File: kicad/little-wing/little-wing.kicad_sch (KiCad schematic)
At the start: 0 parts

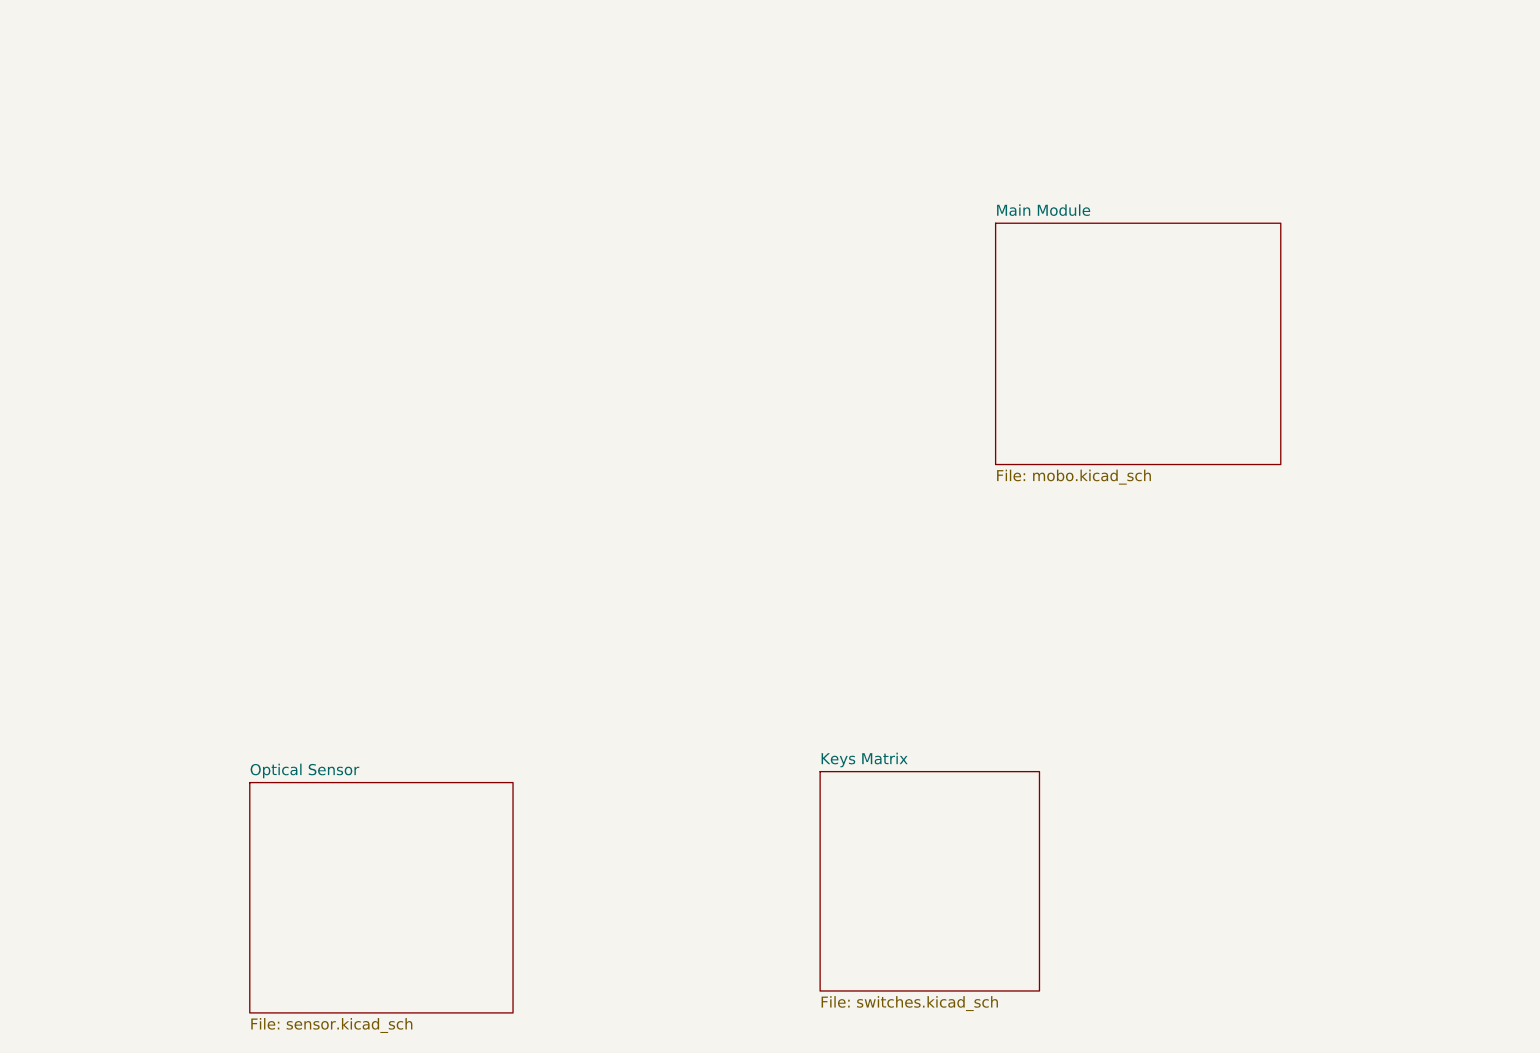
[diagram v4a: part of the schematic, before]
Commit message: Re-organising the schematics sheets a bit
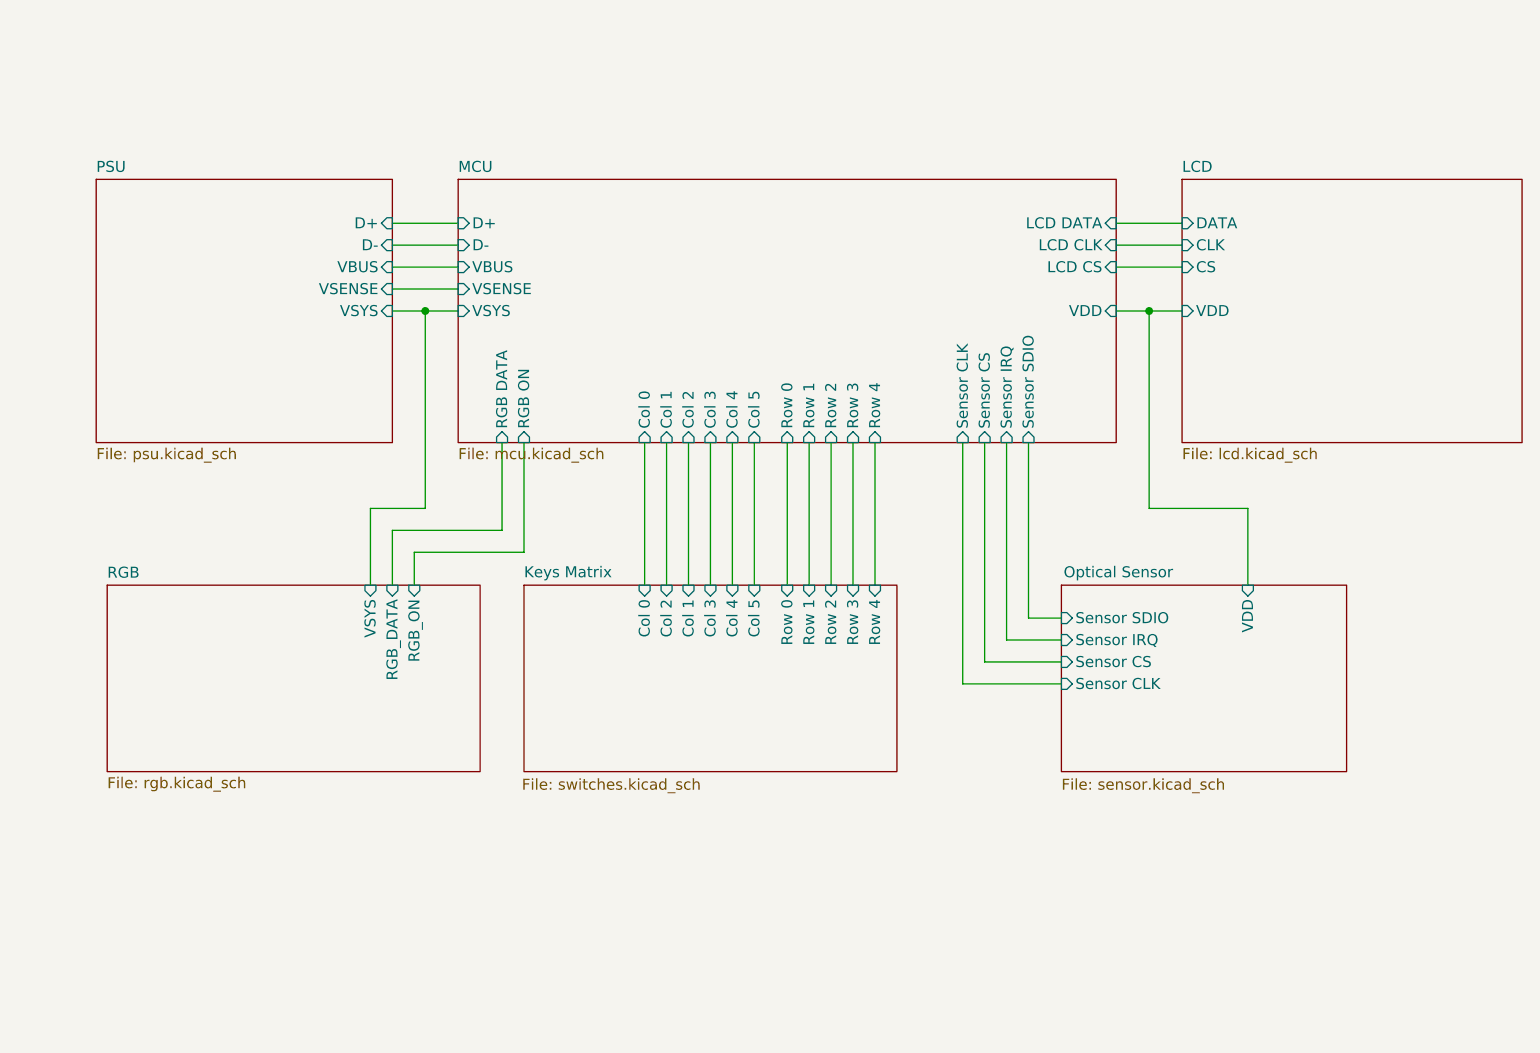
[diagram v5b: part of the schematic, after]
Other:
- removed sheet Main Module
- added sheet LCD (lcd.kicad_sch)
- added sheet MCU (mcu.kicad_sch)
- added sheet PSU (psu.kicad_sch)
- added sheet RGB (rgb.kicad_sch)
- sheet Keys Matrix ports: added Col 0, Col 1, Col 2, Col 3, Col 4, Col 5, Row 0, Row 1, Row 2, Row 3, Row 4; removed none
- sheet Optical Sensor ports: added Sensor CLK, Sensor CS, Sensor IRQ, Sensor SDIO, VDD; removed none

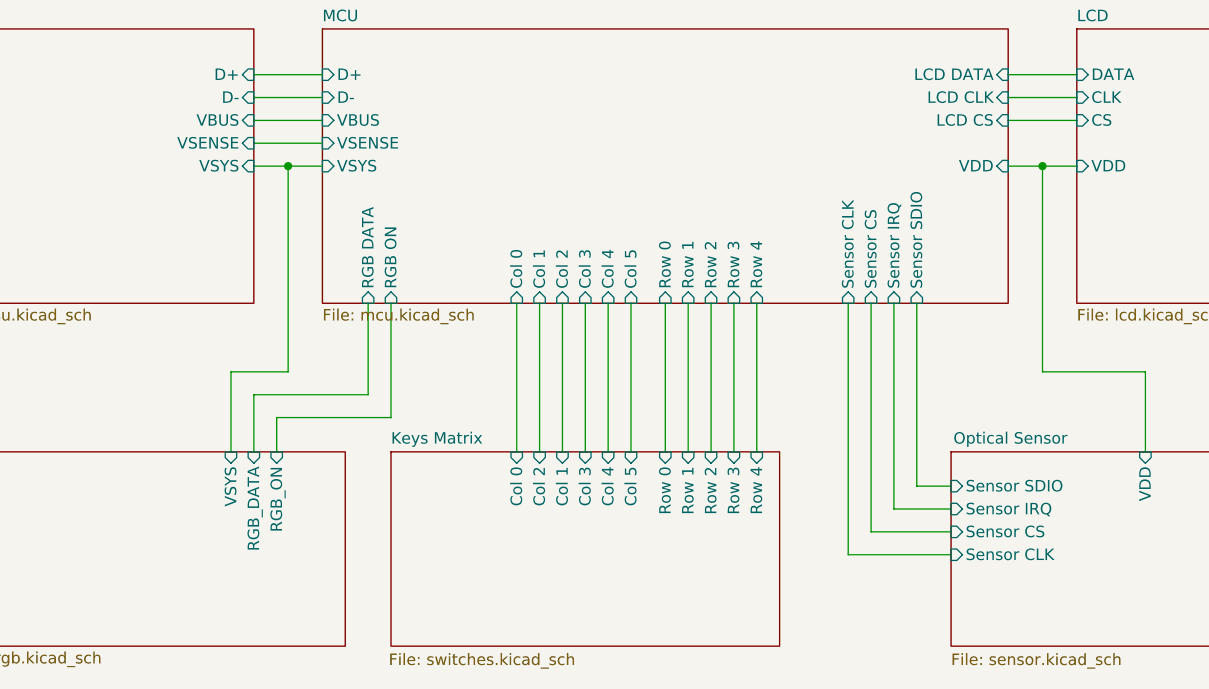
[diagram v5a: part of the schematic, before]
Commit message: Reworking the RGB power section
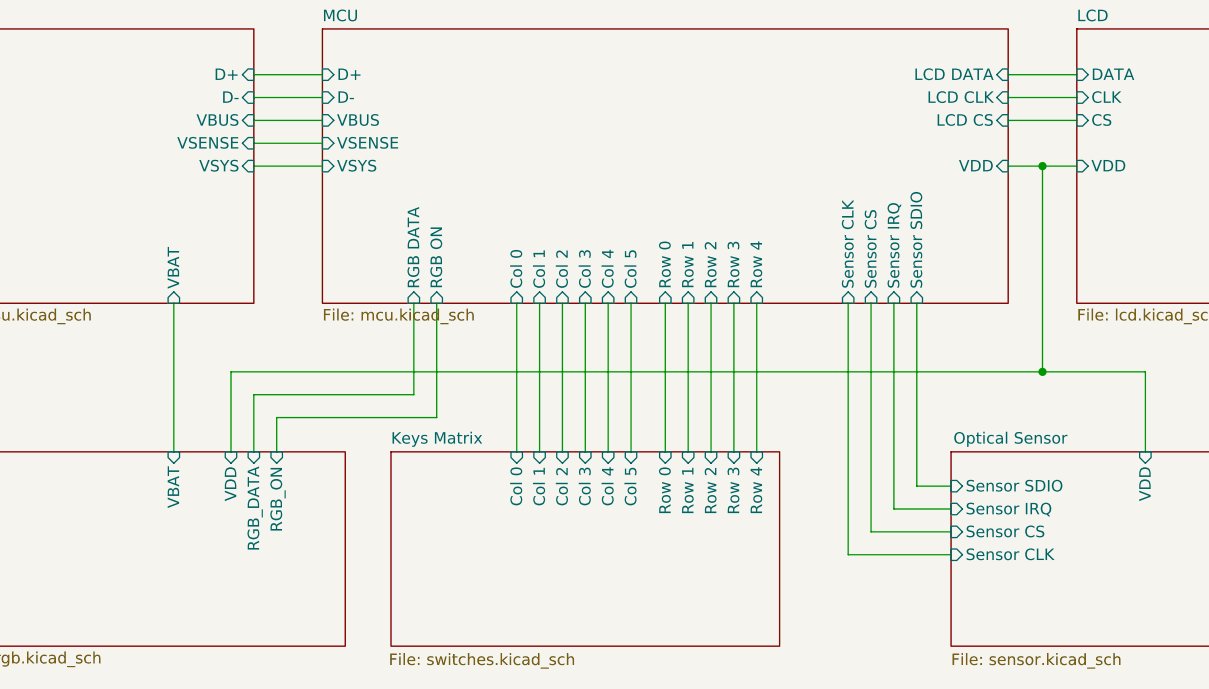
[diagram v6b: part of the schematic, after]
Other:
- sheet PSU ports: added VBAT; removed none
- sheet RGB ports: added VBAT, VDD; removed VSYS
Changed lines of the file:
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@@
 	)
 	(junction
-		(at 147.32 63.5)
+		(at 231.14 86.36)
 		(diameter 0)
 		(color 0 0 0 0)
@@
 	(wire
 		(pts
-			(xy 158.75 91.44) (xy 146.05 91.44)
-		)
-		(stroke
-			(width 0)
-			(type default)
-		)
-	)
-	(wire
-		(pts
-			(xy 140.97 95.25) (xy 140.97 86.36)
+			(xy 163.83 91.44) (xy 146.05 91.44)
 		)
 		(stroke
@@
 	(wire
 		(pts
+			(xy 175.26 78.74) (xy 175.26 95.25)
+		)
+		(stroke
+			(width 0)
+			(type default)
+		)
+	)
+	(wire
+		(pts
 			(xy 242.57 95.25) (xy 242.57 86.36)
 		)
@@
 	(wire
 		(pts
-			(xy 143.51 88.9) (xy 156.21 88.9)
+			(xy 143.51 88.9) (xy 161.29 88.9)
 		)
 		(stroke
@@
 	(wire
 		(pts
-			(xy 175.26 78.74) (xy 175.26 95.25)
-		)
-		(stroke
-			(width 0)
-			(type default)
-		)
-	)
-	(wire
-		(pts
 			(xy 143.51 60.96) (xy 151.13 60.96)
 		)
@@
 	(wire
 		(pts
-			(xy 156.21 88.9) (xy 156.21 78.74)
+			(xy 161.29 88.9) (xy 161.29 78.74)
+		)
+		(stroke
+			(width 0)
+			(type default)
+		)
+	)
+	(wire
+		(pts
+			(xy 143.51 95.25) (xy 143.51 88.9)
+		)
+		(stroke
+			(width 0)
+			(type default)
+		)
+	)
+	(wire
+		(pts
+			(xy 143.51 53.34) (xy 151.13 53.34)
+		)
+		(stroke
+			(width 0)
+			(type default)
+		)
+	)
+	(wire
+		(pts
+			(xy 209.55 78.74) (xy 209.55 106.68)
+		)
+		(stroke
+			(width 0)
+			(type default)
+		)
+	)
+	(wire
+		(pts
+			(xy 231.14 86.36) (xy 140.97 86.36)
+		)
+		(stroke
+			(width 0)
+			(type default)
+		)
+	)
+	(wire
+		(pts
+			(xy 185.42 78.74) (xy 185.42 95.25)
+		)
+		(stroke
+			(width 0)
+			(type default)
+		)
+	)
+	(wire
+		(pts
+			(xy 143.51 63.5) (xy 151.13 63.5)
+		)
+		(stroke
+			(width 0)
+			(type default)
+		)
+	)
+	(wire
+		(pts
+			(xy 199.39 78.74) (xy 199.39 95.25)
+		)
+		(stroke
+			(width 0)
+			(type default)
+		)
+	)
+	(wire
+		(pts
+			(xy 146.05 91.44) (xy 146.05 95.25)
+		)
+		(stroke
+			(width 0)
+			(type default)
+		)
+	)
+	(wire
+		(pts
+			(xy 217.17 99.06) (xy 220.98 99.06)
+		)
+		(stroke
+			(width 0)
+			(type default)
+		)
+	)
+	(wire
+		(pts
+			(xy 163.83 78.74) (xy 163.83 91.44)
+		)
+		(stroke
+			(width 0)
+			(type default)
+		)
+	)
+	(wire
+		(pts
+			(xy 214.63 78.74) (xy 214.63 101.6)
+		)
+		(stroke
+			(width 0)
+			(type default)
+		)
+	)
+	(wire
+		(pts
+			(xy 212.09 78.74) (xy 212.09 104.14)
+		)
+		(stroke
+			(width 0)
+			(type default)
+		)
+	)
+	(wire
+		(pts
+			(xy 143.51 58.42) (xy 151.13 58.42)
 		)
 		(stroke
@@
 	(wire
 		(pts
-			(xy 143.51 95.25) (xy 143.51 88.9)
-		)
-		(stroke
-			(width 0)
-			(type default)
-		)
-	)
-	(wire
-		(pts
-			(xy 143.51 53.34) (xy 151.13 53.34)
-		)
-		(stroke
-			(width 0)
-			(type default)
-		)
-	)
-	(wire
-		(pts
-			(xy 209.55 78.74) (xy 209.55 106.68)
-		)
-		(stroke
-			(width 0)
-			(type default)
-		)
-	)
-	(wire
-		(pts
-			(xy 185.42 78.74) (xy 185.42 95.25)
-		)
-		(stroke
-			(width 0)
-			(type default)
-		)
-	)
-	(wire
-		(pts
-			(xy 147.32 86.36) (xy 147.32 63.5)
-		)
-		(stroke
-			(width 0)
-			(type default)
-		)
-	)
-	(wire
-		(pts
-			(xy 147.32 63.5) (xy 151.13 63.5)
-		)
-		(stroke
-			(width 0)
-			(type default)
-		)
-	)
-	(wire
-		(pts
-			(xy 199.39 78.74) (xy 199.39 95.25)
-		)
-		(stroke
-			(width 0)
-			(type default)
-		)
-	)
-	(wire
-		(pts
-			(xy 146.05 91.44) (xy 146.05 95.25)
-		)
-		(stroke
-			(width 0)
-			(type default)
-		)
-	)
-	(wire
-		(pts
-			(xy 217.17 99.06) (xy 220.98 99.06)
-		)
-		(stroke
-			(width 0)
-			(type default)
-		)
-	)
-	(wire
-		(pts
-			(xy 158.75 78.74) (xy 158.75 91.44)
-		)
-		(stroke
-			(width 0)
-			(type default)
-		)
-	)
-	(wire
-		(pts
-			(xy 214.63 78.74) (xy 214.63 101.6)
-		)
-		(stroke
-			(width 0)
-			(type default)
-		)
-	)
-	(wire
-		(pts
-			(xy 212.09 78.74) (xy 212.09 104.14)
-		)
-		(stroke
-			(width 0)
-			(type default)
-		)
-	)
-	(wire
-		(pts
-			(xy 143.51 58.42) (xy 151.13 58.42)
-		)
-		(stroke
-			(width 0)
-			(type default)
-		)
-	)
-	(wire
-		(pts
 			(xy 212.09 104.14) (xy 220.98 104.14)
 		)
@@
 	(wire
 		(pts
-			(xy 140.97 86.36) (xy 147.32 86.36)
+			(xy 140.97 86.36) (xy 140.97 95.25)
 		)
 		(stroke
@@
 	(wire
 		(pts
-			(xy 143.51 63.5) (xy 147.32 63.5)
+			(xy 134.62 78.74) (xy 134.62 95.25)
 		)
 		(stroke
@@
 		)
 		(pin "RGB DATA" input
-			(at 156.21 78.74 270)
+			(at 161.29 78.74 270)
 			(effects
 				(font
@@
 		)
 		(pin "RGB ON" input
-			(at 158.75 78.74 270)
+			(at 163.83 78.74 270)
 			(effects
 				(font
@@
 			)
 		)
-		(pin "VSYS" input
+		(pin "VBAT" input
+			(at 134.62 95.25 90)
+			(effects
+				(font
+					(size 1.27 1.27)
+				)
+				(justify right)
+			)
+		)
+		(pin "VDD" input
 			(at 140.97 95.25 90)
 			(effects
@@
 			)
 		)
+		(pin "VBAT" input
+			(at 134.62 78.74 270)
+			(effects
+				(font
+					(size 1.27 1.27)
+				)
+				(justify left)
+			)
+		)
 		(instances
 			(project "little-wing"
@@
 		)
 		(pin "Col 1" input
-			(at 177.8 95.25 90)
+			(at 175.26 95.25 90)
 			(effects
 				(font
@@
 		)
 		(pin "Col 2" input
-			(at 175.26 95.25 90)
-			(effects
-				(font
+			(at 177.8 95.25 90)
+			(effects
+				(font

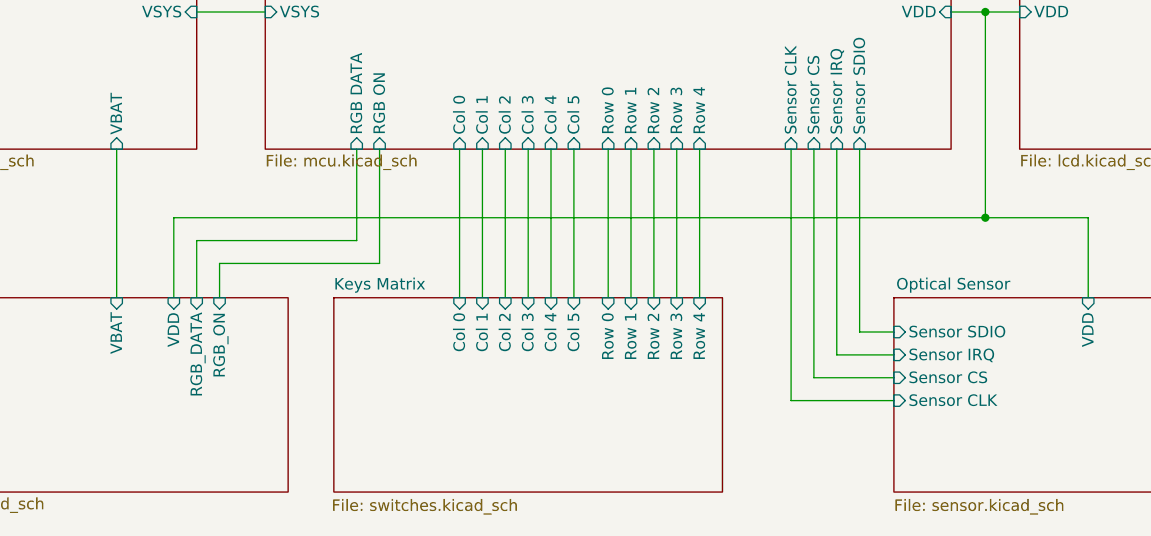
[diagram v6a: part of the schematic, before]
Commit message: Removing the RGB level shifter
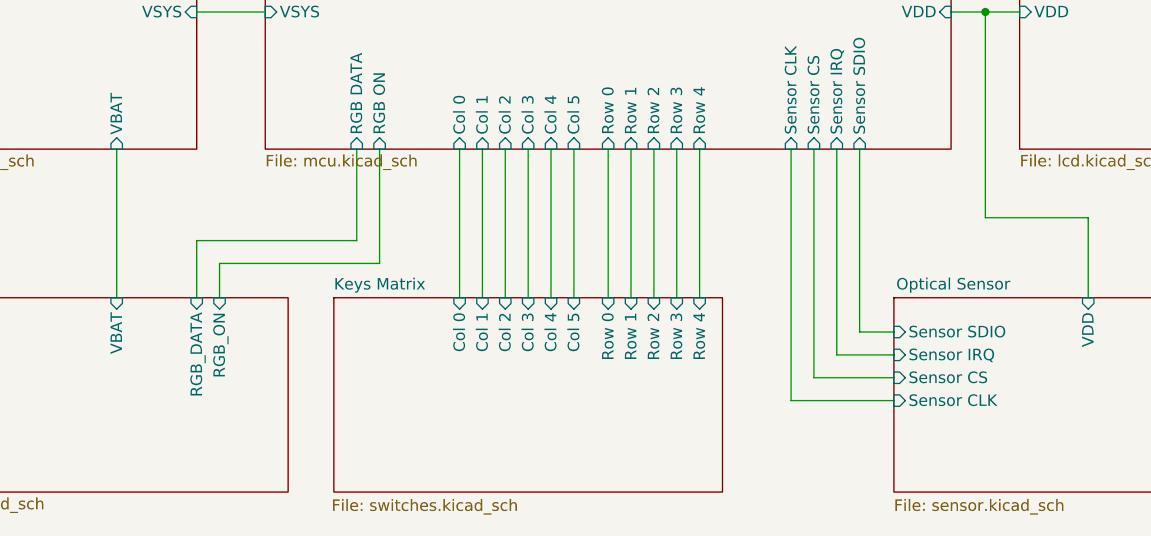
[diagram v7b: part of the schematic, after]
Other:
- sheet RGB ports: added none; removed VDD
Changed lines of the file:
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@@
 		(color 0 0 0 0)
 	)
-	(junction
-		(at 231.14 86.36)
-		(diameter 0)
-		(color 0 0 0 0)
-	)
 	(wire
 		(pts
@@
 	(wire
 		(pts
-			(xy 231.14 86.36) (xy 140.97 86.36)
-		)
-		(stroke
-			(width 0)
-			(type default)
-		)
-	)
-	(wire
-		(pts
 			(xy 185.42 78.74) (xy 185.42 95.25)
 		)
@@
 		(pts
 			(xy 209.55 106.68) (xy 220.98 106.68)
-		)
-		(stroke
-			(width 0)
-			(type default)
-		)
-	)
-	(wire
-		(pts
-			(xy 140.97 86.36) (xy 140.97 95.25)
 		)
 		(stroke
@@
 			(effects
 				(font
-					(size 1.27 1.27)
-				)
-				(justify right)
-			)
-		)
-		(pin "VDD" input
-			(at 140.97 95.25 90)
-			(effects
-				(font
